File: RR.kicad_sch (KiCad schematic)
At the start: 41 parts, among them J16 Conn_01x01_Pin, J17 Conn_01x01_Pin, J18 Conn_01x01_Pin, Q31 NMOS, Q32 NMOS, Q33 NMOS, Q34 NMOS, Q35 NMOS, Q36 NMOS, U11 OPA2196xDGK, U12 MCT8329A1IREER

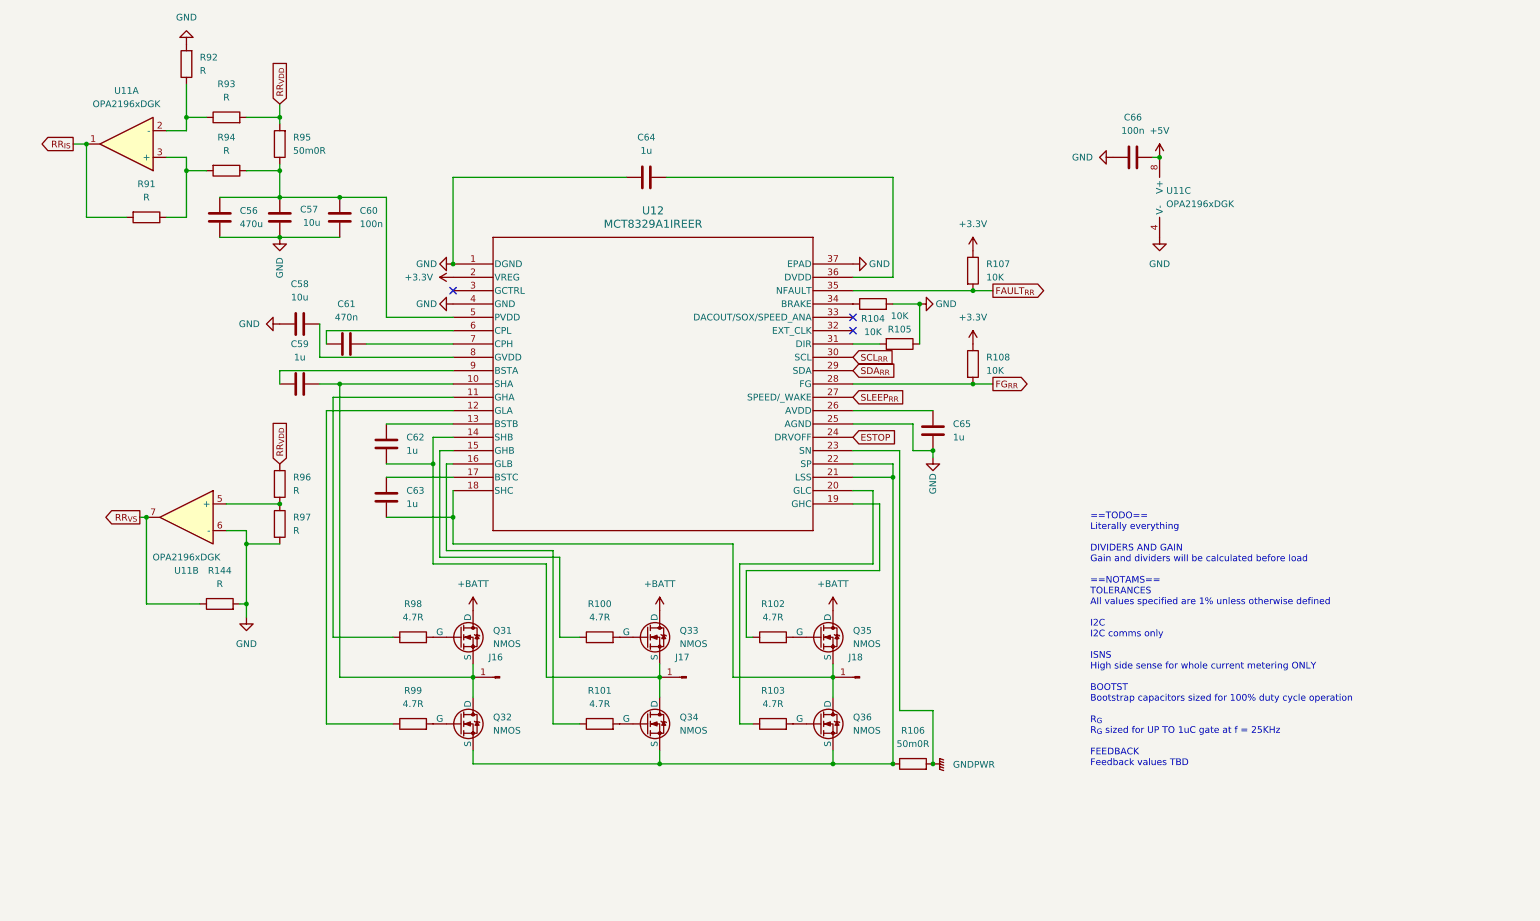
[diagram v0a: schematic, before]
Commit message: The great decluttering
Moved all possible controls to I2C, part selection commenced, IOs assigned pending comms schema
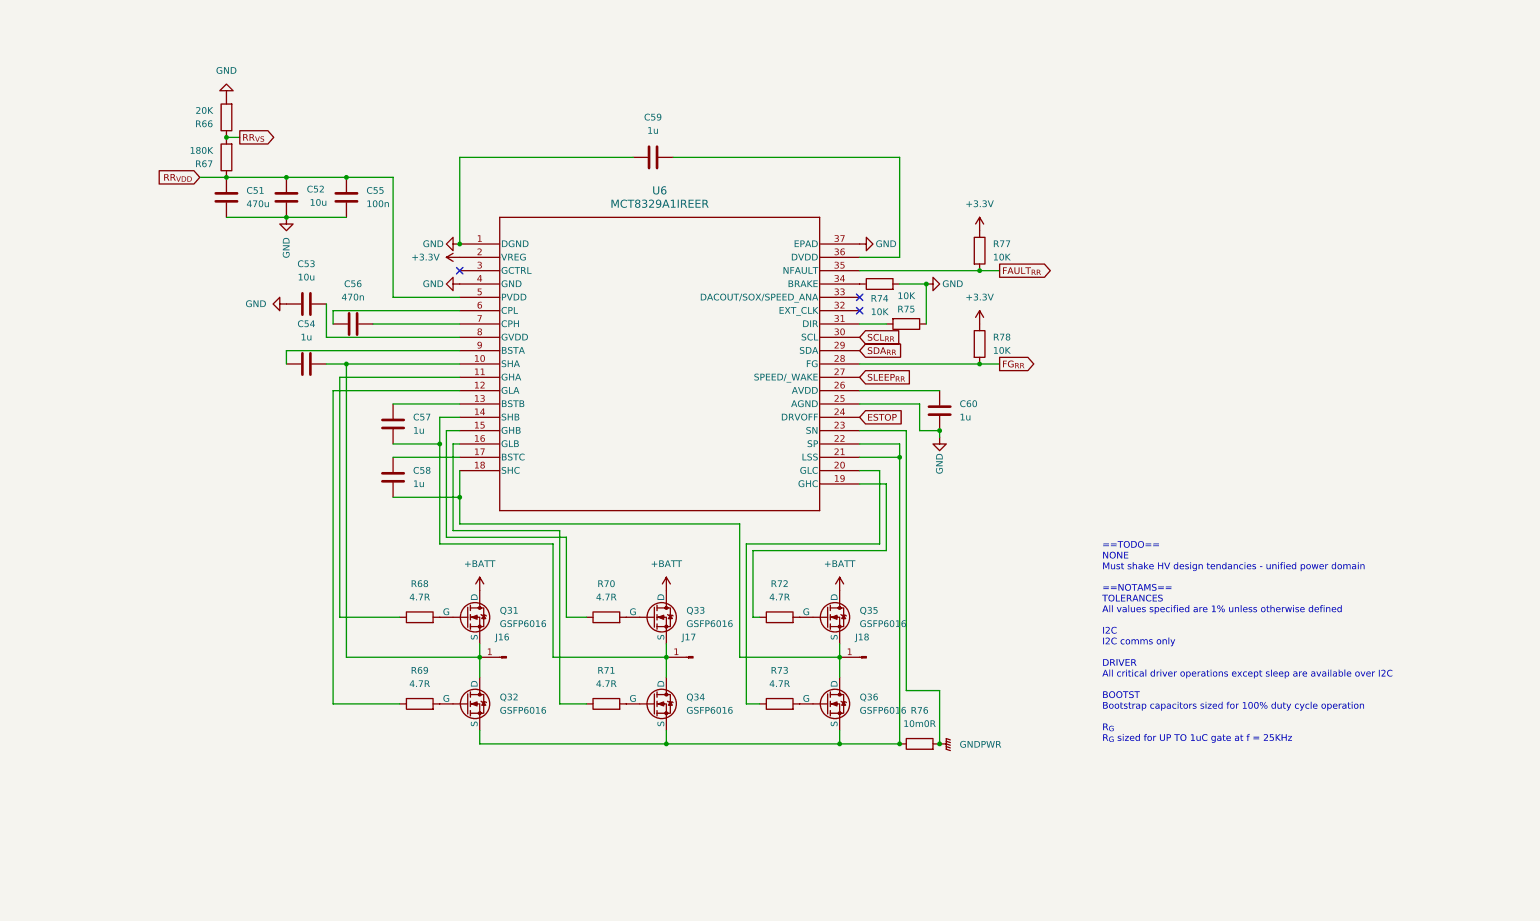
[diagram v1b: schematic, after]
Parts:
- removed C61: 470n, Capacitor_SMD:C_0603_1608Metric, symbol Device:C
- removed C62, C63, C64, C65: 1u, Capacitor_SMD:C_0603_1608Metric, symbol Device:C
- removed C66: 100n, Capacitor_SMD:C_0603_1608Metric, symbol Device:C
- removed R100, R101, R102, R103, R98, R99: 4.7R, Resistor_SMD:R_1206_3216Metric, symbol Device:R
- removed R104, R105, R107, R108: 10K, Resistor_SMD:R_0603_1608Metric_Pad0.98x0.95mm_HandSolder, symbol Device:R
- removed R106, R95: 50m0R, Resistor_SMD:R_1206_3216Metric, symbol Device:R
- removed R144, R91, R92, R93, R94, R96, R97: R, Resistor_SMD:R_0603_1608Metric_Pad0.98x0.95mm_HandSolder, symbol Device:R
- removed U11: OPA2196xDGK, Package_SO:VSSOP-8_3x3mm_P0.65mm, symbol Amplifier_Operational:OPA2196xDGK
- removed U12: MCT8329A1IREER, footprints:WQFN36_REE_TEX, symbol MCT8329:MCT8329A1IREER
- added C51: 470u, Capacitor_SMD:C_0603_1608Metric, symbol Device:C
- added C52, C53: 10u, Capacitor_SMD:C_0603_1608Metric, symbol Device:C
- added C54: 1u, Capacitor_SMD:C_0603_1608Metric, symbol Device:C
- added C55: 100n, Capacitor_SMD:C_0603_1608Metric, symbol Device:C
- added R66: 20K, Resistor_SMD:R_0603_1608Metric_Pad0.98x0.95mm_HandSolder, symbol Device:R
- added R67: 180K, Resistor_SMD:R_0603_1608Metric_Pad0.98x0.95mm_HandSolder, symbol Device:R
- added R68, R69, R70, R71, R72, R73: 4.7R, Resistor_SMD:R_1206_3216Metric, symbol Device:R
- added R74, R75, R77, R78: 10K, Resistor_SMD:R_0603_1608Metric_Pad0.98x0.95mm_HandSolder, symbol Device:R
- added R76: 10m0R, Resistor_SMD:R_1206_3216Metric, symbol Device:R
- added U6: MCT8329A1IREER, footprints:WQFN36_REE_TEX, symbol MCT8329:MCT8329A1IREER
- C56: value 470u -> 470n
- C57, C58: value 10u -> 1u
- C60: value 100n -> 1u
- Q31, Q32, Q33, Q34, Q35, Q36: value NMOS -> GSFP6016; footprint (none) -> Package_DFN_QFN:PQFN-8-EP_6x5mm_P1.27mm_Generic
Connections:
- net +3.3V: now also R77.1, R78.1, U6.2 (VREG)
- net ESTOP: now also U6.24 (DRVOFF)
- net FAULT_{RR}: now also R77.2, U6.35 (NFAULT)
- net FG_{RR}: now also R78.2, U6.28 (FG)
- net GND: now also C59.1, C60.1, C51.2, C52.2, C53.1, C55.2, R66.2, R74.2, R75.1, U6.1 (DGND), U6.25 (AGND), U6.37 (EPAD), U6.4 (GND); no longer C56.2, C57.2, C58.1, C60.2
- net GNDPWR: now also R76.2, U6.23 (SN)
- net RR_{VDD}: now also C51.1, C52.1, C55.1, R67.1, U6.5 (PVDD)
- net RR_{VS}: now also R66.1, R67.2
- net SCL_{RR}: now also U6.30 (SCL)
- net SDA_{RR}: now also U6.29 (SDA)
- net SLEEP_{RR}: now also U6.27 (SPEED/_WAKE)
- net at Q32.2 (G): now also R69.2
- net at Q36.2 (G): now also R73.2
- net at J18.1 (Pin_1), Q35.3 (S), Q36.1 (D): now also C58.2, U6.18 (SHC)
- net at J17.1 (Pin_1), Q33.3 (S), Q34.1 (D): now also C57.2, U6.14 (SHB)
- net at Q34.2 (G): now also R71.2
- net at Q31.2 (G): now also R68.2
- net at J16.1 (Pin_1), Q31.3 (S), Q32.1 (D): now also C54.1, U6.10 (SHA); no longer C59.1
- net at Q32.3 (S), Q34.3 (S), Q36.3 (S): now also R76.1, U6.21 (LSS), U6.22 (SP)
- net at Q33.2 (G): now also R70.2
- net at Q35.2 (G): now also R72.2
- net at C59.2: now also U6.36 (DVDD)
- new net: C58.1, U6.17 (BSTC)
- new net: R71.1, U6.16 (GLB)
- new net: C56.1, U6.6 (CPL)
- new net: C56.2, U6.7 (CPH)
- new net: R75.2, U6.31 (DIR)
- new net: C57.1, U6.13 (BSTB)
- new net: C54.2, U6.9 (BSTA)
- new net: R70.1, U6.15 (GHB)
- new net: R68.1, U6.11 (GHA)
- new net: C60.2, U6.26 (AVDD)
- new net: R74.1, U6.34 (BRAKE)
- new net: R73.1, U6.20 (GLC)
- new net: C53.2, U6.8 (GVDD)
- new net: R69.1, U6.12 (GLA)
- new net: R72.1, U6.19 (GHC)
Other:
- note added: "==TODO== NONE Must shake HV design tendancies - unified power domain ==NOTAMS== TOLERANCES All values specified are 1% unless otherwise defined I2C I2C comms only DRIVER All critical driver operations except sleep are available over I2C BOOTST Bootstrap capacitors sized for 100% duty cycle operation R_{G} R_{G} sized for UP TO 1uC gate at f = 25KHz"
- note removed: "==TODO== Literally everything DIVIDERS AND GAIN Gain and dividers will be calculated before load ==NOTAMS== TOLERANCES All values specified are 1% unless otherwise defined I2C I2C comms only ISNS High side sense for whole current metering ONLY BOOTST Bootstrap capacitors sized for 100% duty cycle operation R_{G} R_{G} sized for UP TO 1uC gate at f = 25KHz FEEDBACK Feedback values TBD"

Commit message: Powerstage
Powerstage layout, non critical changes to schematic
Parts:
- removed C55: 100n, Capacitor_SMD:C_0603_1608Metric, symbol Device:C
- removed J16, J17, J18: Conn_01x01_Pin, symbol Connector:Conn_01x01_Pin
- removed Q31, Q32, Q33, Q34, Q35, Q36: GSFP6016, Package_DFN_QFN:PQFN-8-EP_6x5mm_P1.27mm_Generic, symbol Simulation_SPICE:NMOS
- removed R76: 10m0R, Resistor_SMD:R_1206_3216Metric, symbol Device:R
- added J6: 1724470408, footprints:CONN08_1724470408_MOL, symbol 1724470408:1724470408
- added Q31, Q32, Q33, Q34, Q35, Q36: GSFP6016, Package_SO:PowerPAK_SO-8_Single, symbol Transistor_FET:SiR696DP
- added R76: WSL3637R0100FEA, WSL3637_VIS, symbol WSL3637R0100FEA:WSL3637R0100FEA
- C51: footprint Capacitor_SMD:C_0603_1608Metric -> Capacitor_THT:CP_Radial_D10.0mm_P5.00mm
- C52: footprint Capacitor_SMD:C_0603_1608Metric -> Capacitor_SMD:C_1210_3225Metric
- C53: footprint Capacitor_SMD:C_0603_1608Metric -> Capacitor_SMD:C_0402_1005Metric
- C54, C56, C57, C58, C59, C60: footprint Capacitor_SMD:C_0603_1608Metric -> Capacitor_SMD:C_0201_0603Metric
- R66, R67, R74, R75, R77, R78: footprint Resistor_SMD:R_0603_1608Metric_Pad0.98x0.95mm_HandSolder -> Resistor_SMD:R_0201_0603Metric
- R68, R69, R70, R71, R72, R73: value 4.7R -> 4R7; footprint Resistor_SMD:R_1206_3216Metric -> Resistor_SMD:R_0603_1608Metric
- U6: footprint footprints:WQFN36_REE_TEX -> WQFN36_REE_TEX
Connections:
- net GNDPWR: now also J6.4, J6.8, R76.4; no longer U6.23 (SN)
- net RR_{VDD}: now also Q31.5 (D), Q33.5 (D), Q35.5 (D)
- net at R68.2: now also Q31.4 (G)
- net at C54.1, U6.10 (SHA): now also J6.1, J6.5, Q31.1 (S), Q31.2 (S), Q31.3 (S), Q32.5 (D)
- net at C58.2, U6.18 (SHC): now also J6.3, J6.7, Q35.1 (S), Q35.2 (S), Q35.3 (S), Q36.5 (D)
- net at R72.2: now also Q35.4 (G)
- net at R71.2: now also Q34.4 (G)
- net at C57.2, U6.14 (SHB): now also J6.2, J6.6, Q33.1 (S), Q33.2 (S), Q33.3 (S), Q34.5 (D)
- net at C56.1: now also U6.7 (CPH); no longer U6.6 (CPL)
- net at C56.2: now also U6.6 (CPL); no longer U6.7 (CPH)
- net at R70.2: now also Q33.4 (G)
- net at U6.21 (LSS), U6.22 (SP): now also R76.2
- net at R69.2: now also Q32.4 (G)
- net at R73.2: now also Q36.4 (G)
- new net: Q32.1 (S), Q32.2 (S), Q32.3 (S), Q34.1 (S), Q34.2 (S), Q34.3 (S), Q36.1 (S), Q36.2 (S), Q36.3 (S), R76.1
- new net: R76.3, U6.23 (SN)
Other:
- note added: "==TODO== NONE Must shake HV design tendancies - unified power domain ==NOTAMS== TOLERANCES All values specified are 1% unless otherwise defined I2C I2C comms only DRIVER All critical driver operations except sleep are available over I2C BOOTST Bootstrap capacitors sized for 100% duty cycle operation R_{G} R_{G} sized for UP TO 1uC gate at f = 25KHz SUBSTRATE TEMP PCB will not comply with IEC boar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"
- note removed: "==TODO== NONE Must shake HV design tendancies - unified power domain ==NOTAMS== TOLERANCES All values specified are 1% unless otherwise defined I2C I2C comms only DRIVER All critical driver operations except sleep are available over I2C BOOTST Bootstrap capacitors sized for 100% duty cycle operation R_{G} R_{G} sized for UP TO 1uC gate at f = 25KHz"
